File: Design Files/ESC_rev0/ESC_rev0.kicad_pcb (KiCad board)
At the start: 4 copper layers, 100 x 75 mm, 175 parts, among them J1 Conn_01x08, J2 Conn_01x06, J3 Conn_01x03, J4 WP-BUTR, J5 WP-BUTR, J6 WP-BUTR, J7 Conn_01x04, J8 Conn_01x06, J9 USB_C_Receptacle_USB2.0_16P, Q1 HSBA15810C, Q2 HSBA15810C, Q3 HSBA15810C, Q4 HSBA15810C, Q5 HSBA15810C, Q6 HSBA15810C, SW1 Push Button, U1 XT60PW-M, U2 XH-2PWBPZ, U3 AMS1117-3.3, U4 STM32F405RGTx, U5 DRV8302DCA, U6 ESDCAN24-2BLY, U7 SN65HVD230, Y1 Crystal

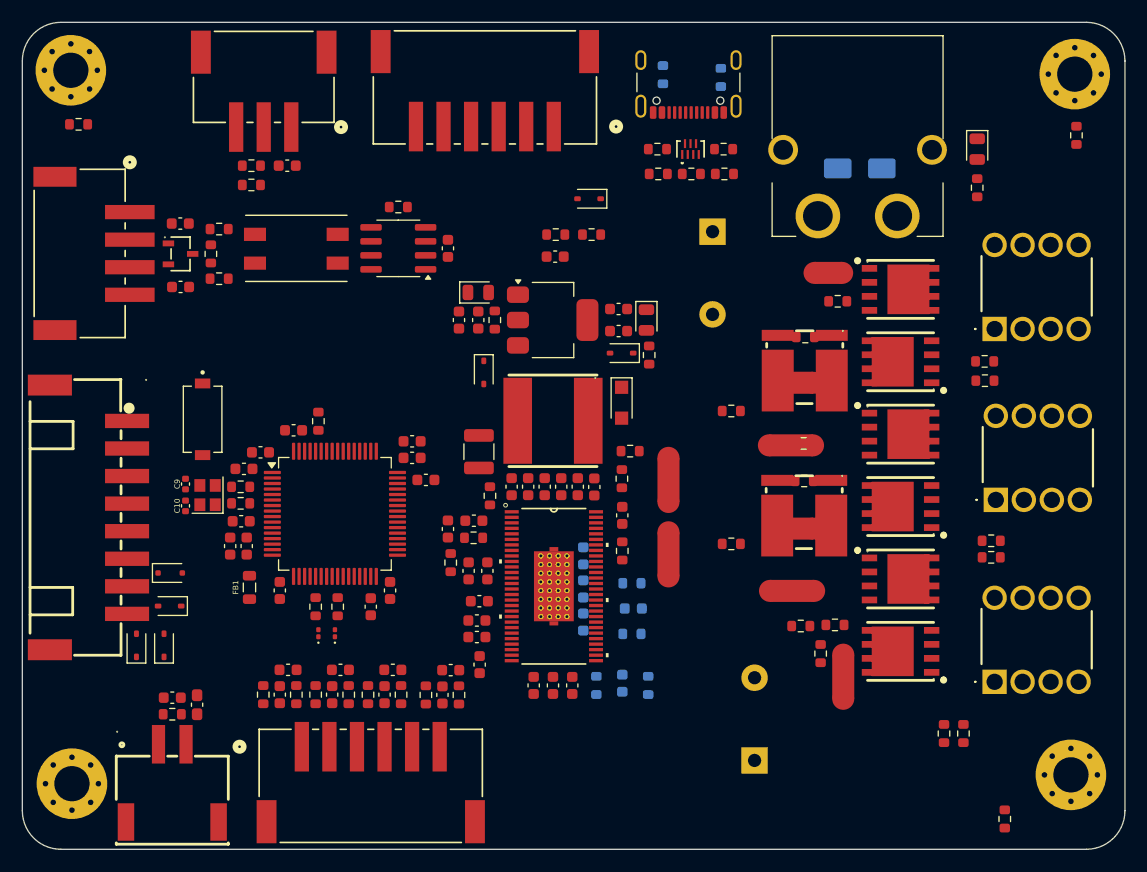
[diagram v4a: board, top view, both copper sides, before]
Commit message: update 18
Route process partially complete. Some corrections were made in footprints and pins references. Probably the power lines will need changes in size.
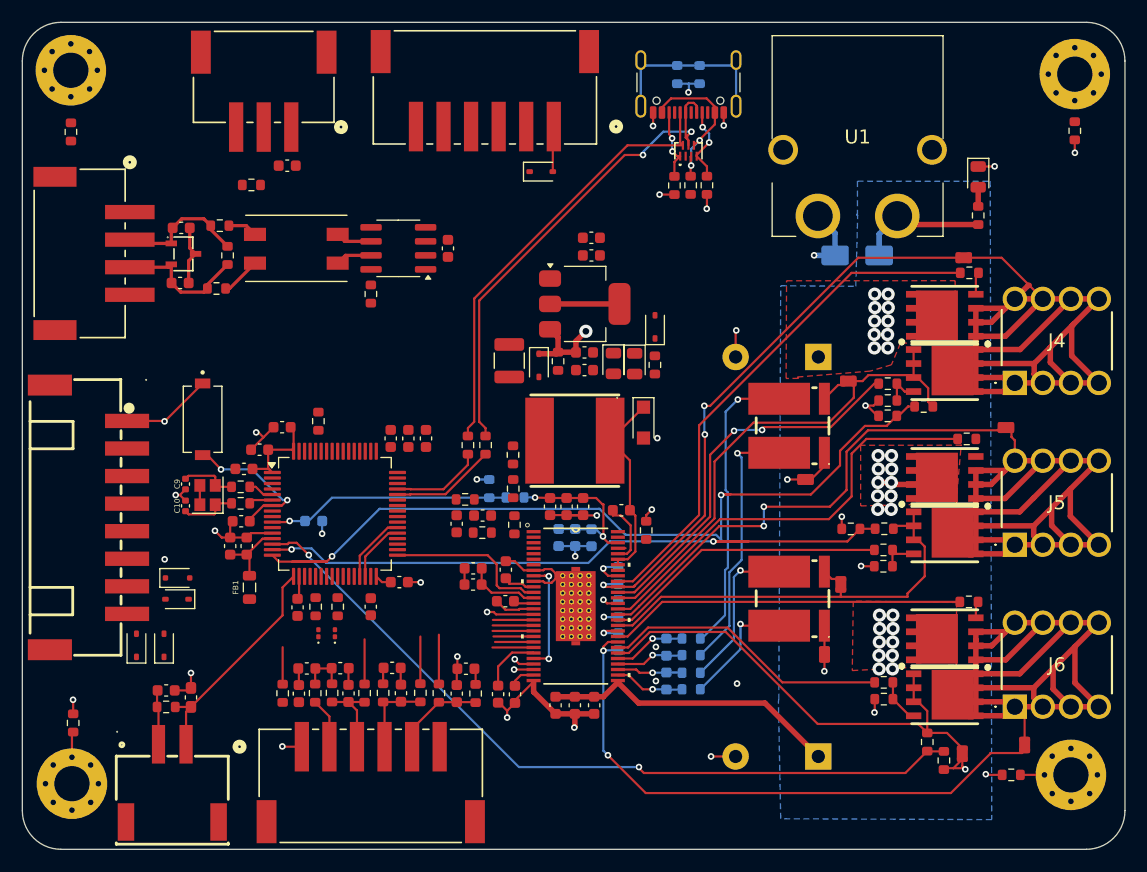
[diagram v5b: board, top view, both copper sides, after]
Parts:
- C38, C4, C44, C45, R2, R27, R3, R33, R52: moved to B.Cu
- NT1, NT2, NT5: footprint NetTie:NetTie-2_SMD_Pad2.00mm_Small -> NetTie:NetTie-2_SMD_Pad1.0mm_custom
- NT3, NT4, NT6, NT7, NT8: footprint NetTie:NetTie-2_SMD_Pad2.0mm -> NetTie:NetTie-2_SMD_Pad1.0mm_custom
- R29, R35, R54: moved to F.Cu
- moved R60 90.4 mm to (175.0, 64.9), turned to -90 degrees
- moved R62 84.9 mm to (84.2, 118.6), turned to 90 degrees
- moved R40 64.5 mm to (98.2, 76.2), turned to 90 degrees
- moved R52 61.5 mm to (141.0, 59.8), turned to -90 degrees
- moved R61 58.3 mm to (169.3, 123.3), turned to 180 degrees
- moved R59 53.2 mm to (84.0, 65.0), turned to -90 degrees
- moved R44 44.1 mm to (112.3, 115.9), turned to -90 degrees
- moved R19 36.6 mm to (161.7, 120.3)
- moved R13 35.9 mm to (119.8, 98.3), turned to 0 degrees
- moved R58 35.5 mm to (120.0, 93.4), turned to -90 degrees
- moved R57 32.8 mm to (121.6, 93.4), turned to -90 degrees
- moved C4 32.5 mm to (106.0, 100.3), turned to 0 degrees
- moved R27 29.2 mm to (140.2, 111.0)
- moved R29 28.5 mm to (158.1, 89.4)
- moved NT7 25.3 mm to (170.5, 120.6), turned to 90 degrees
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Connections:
- C38 pad 2: Net-(C38-Pad2) -> GND
- C40 pad 2: Net-(C38-Pad2) -> GND
- C41 pad 2: Net-(C38-Pad2) -> GND
- C42 pad 2: Net-(C38-Pad2) -> GND
- C44 pad 2: Net-(C38-Pad2) -> GND
- C45 pad 2: Net-(C38-Pad2) -> GND
- C53 pad 1: +3.3V -> +3V3
- C54 pad 1: +3.3V -> +3V3
- C57 pad 1: +3.3V -> +3V3
- C58 pad 1: +3.3V -> +3V3
- R44 pad 1: +3.3V -> +3V3
- R45 pad 1: +3.3V -> +3V3
- R48 pad 1: +3.3V -> +3V3
- R49 pad 1: +3.3V -> +3V3
- U1 pad 1: +VDC -> GND
- U1 pad 2: GND -> +VDC
- U4 pad 26: BR_S02 -> BR_SO2
- U4 pad 27: BR_S01 -> BR_SO1
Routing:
- net GND: track 0.00 -> 114.7 mm, vias 0 -> 39
- net /MOSFETs/PHASE_1: track 0.00 -> 92.8 mm
- net /MOSFETs/PHASE_3: track 0.00 -> 86.2 mm
- net /MOSFETs/PHASE_2: track 0.00 -> 84.4 mm
- net SENS1: track 0.00 -> 73.9 mm, vias 0 -> 2
- net SENS3: track 0.00 -> 70.8 mm, vias 0 -> 2
- net SENS2: track 0.00 -> 59.9 mm, vias 0 -> 2
- net +VDC: track 0.00 -> 59.5 mm, vias 0 -> 10
- net SH3: track 0.00 -> 53.7 mm, vias 0 -> 2
- net SH1: track 0.00 -> 51.9 mm, vias 0 -> 3
- net GH1: track 0.00 -> 47.4 mm
- net SH2: track 0.00 -> 46.4 mm, vias 0 -> 3
- net SL1: track 0.00 -> 45.3 mm
- net /USB/USB-C_N: track 0.00 -> 44.6 mm, vias 0 -> 2
- net SL3: track 0.00 -> 42.5 mm
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- added copper zone on B.Cu, net +VDC
- added copper zone on F.Cu, net +VDC

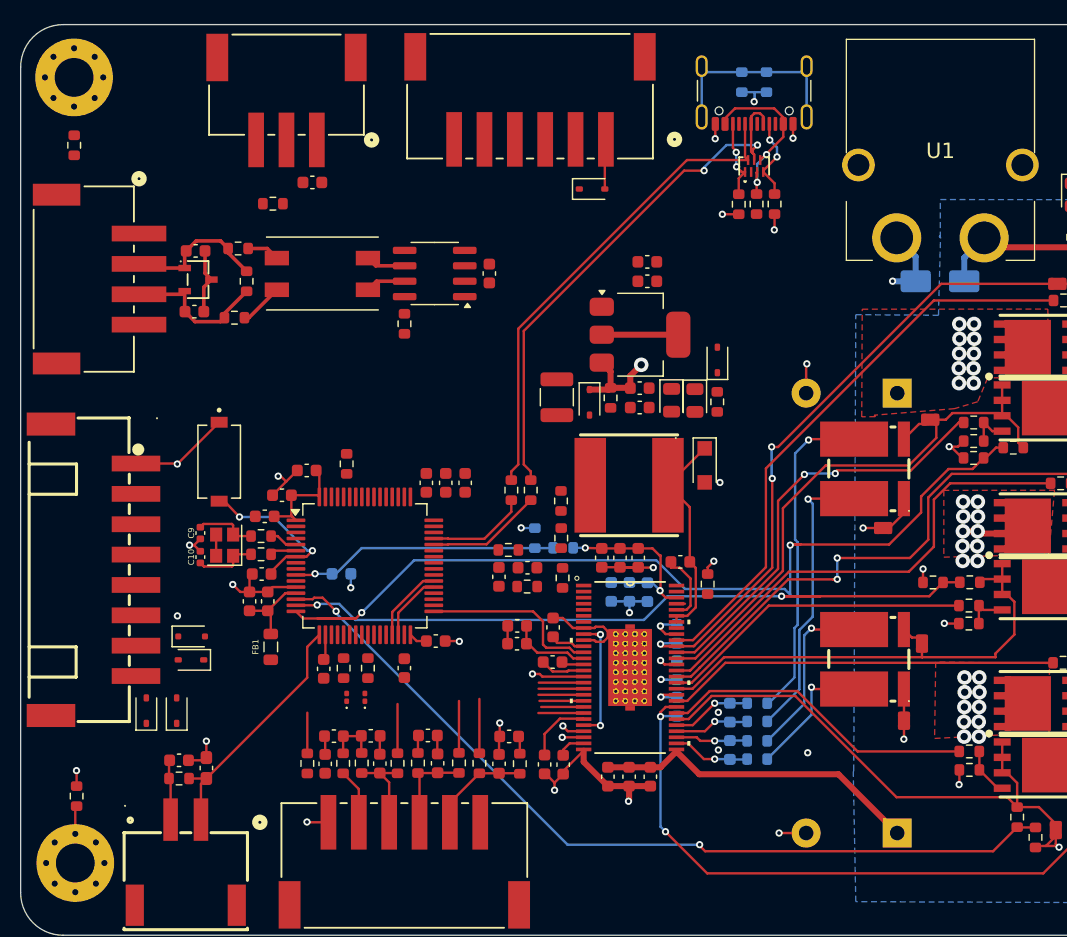
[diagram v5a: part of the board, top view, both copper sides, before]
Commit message: update 19
Preliminary routing finished, all signaling connections made.
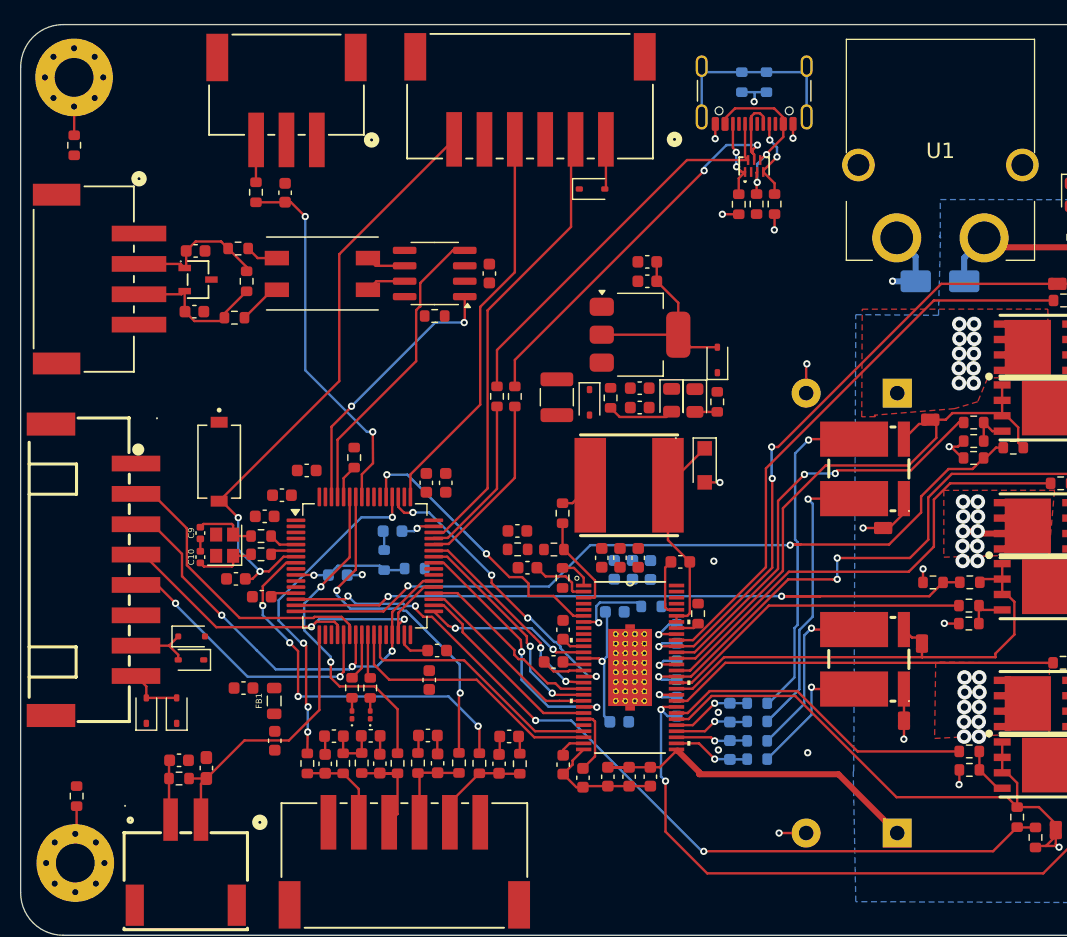
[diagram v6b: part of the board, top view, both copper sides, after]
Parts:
- C18, C26, C28, R14: moved to B.Cu
- moved R3 12.5 mm to (109.5, 99.2)
- moved R2 12.3 mm to (112.0, 99.9)
- moved C26 11.5 mm to (128.9, 112.5), turned to 0 degrees
- moved R14 10.4 mm to (131.5, 103.0), turned to 180 degrees
- moved C28 8.47 mm to (128.5, 103.4), turned to 0 degrees
- moved R57 7.83 mm to (120.3, 85.7)
- moved R58 7.81 mm to (118.8, 85.7)
- moved C18 7.18 mm to (110.2, 96.8), turned to 180 degrees
- moved C14 7.16 mm to (100.5, 114.0), turned to -90 degrees
- moved C22 7.16 mm to (97.9, 109.7), turned to 180 degrees
- moved FB1 4.46 mm to (100.5, 110.8)
- moved C27 4.07 mm to (120.5, 96.8), turned to 180 degrees
- moved C24 3.35 mm to (125.9, 117.1)
- moved C19 3.26 mm to (113.2, 109.0), turned to -90 degrees
- moved C16 3.06 mm to (113.9, 106.6), turned to 0 degrees
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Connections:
- U4 pad 61: /MCU/CAN_RX -> CAN_RX
- U4 pad 62: /MCU/CAN_TX -> CAN_TX
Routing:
- net GND: track 114.7 -> 57.0 mm, vias 39 -> 24
- net /MCU/SWDIO: track 0.00 -> 37.7 mm
- net /MCU/NRST: track 13.9 -> 50.0 mm
- net /MCU/SWCLK: track 0.00 -> 33.0 mm
- net /MCU/RX_SCL_MOSI: track 6.36 -> 38.3 mm, vias 0 -> 3
- net /MCU/SERVO: track 0.00 -> 30.6 mm, vias 0 -> 2
- net /MCU/TX_SDA_NSS: track 5.61 -> 35.9 mm, vias 0 -> 2
- net TEMP_OUT: track 4.47 -> 32.2 mm, vias 0 -> 4
- net CAN_RX: track 0.00 -> 25.2 mm
- net /MCU/MISO_ADC_EXT2: track 0.00 -> 24.7 mm
- net HALL_1_OUT: track 4.28 -> 28.9 mm, vias 0 -> 2
- net HALL_3_OUT: track 3.35 -> 27.7 mm, vias 0 -> 4
- net /MCU/SCK_ADC_EXT: track 0.00 -> 23.8 mm, vias 0 -> 2
- net FAULT: track 0.00 -> 23.7 mm, vias 0 -> 2
- net HALL_2_OUT: track 4.05 -> 27.4 mm, vias 0 -> 2
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
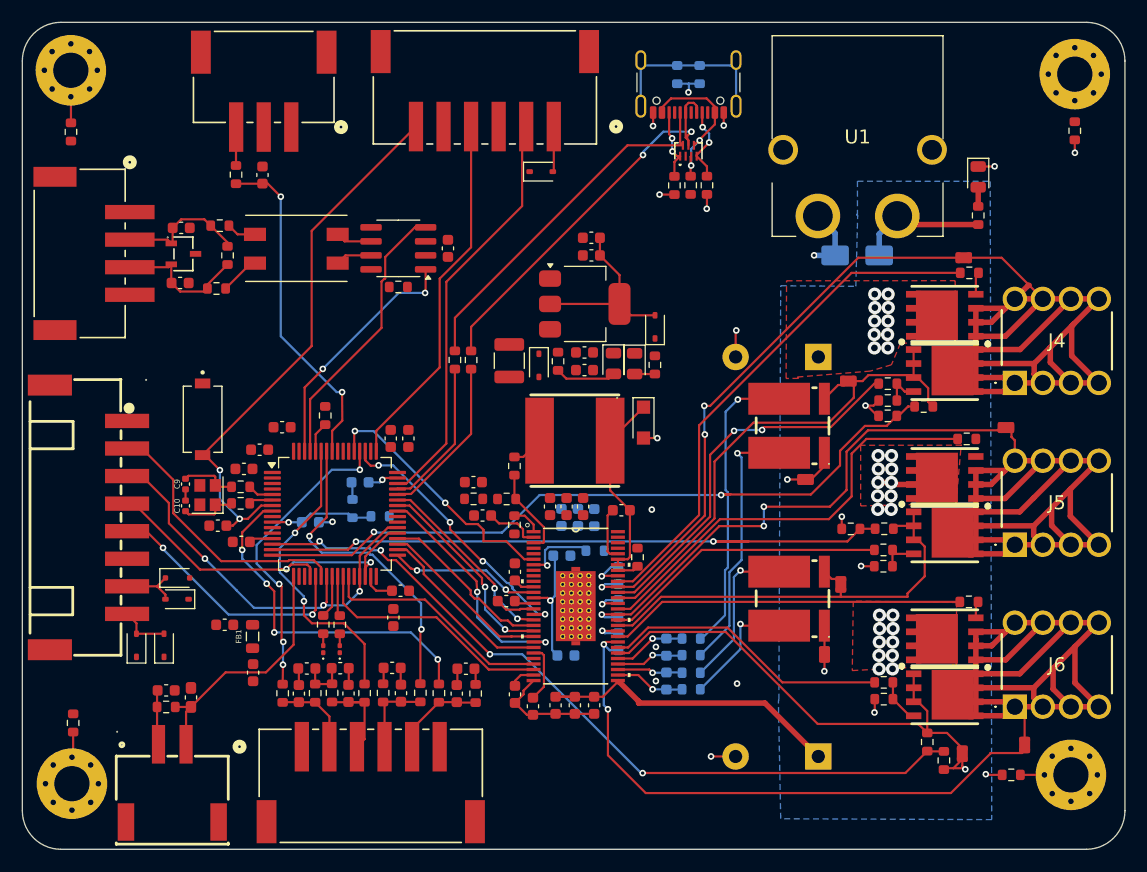
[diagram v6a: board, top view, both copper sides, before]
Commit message: update 20
Tracing complete (some power tracks need to be validated and some others optimizations weren't made). All connections were made, reference planes created, copper pour on mosfets and other power pads (not all). Some tracks were modified. References visible and apparently ok (it's just demo). Stitching vias were applied all over the board. Informative texts and symbols weren't included.
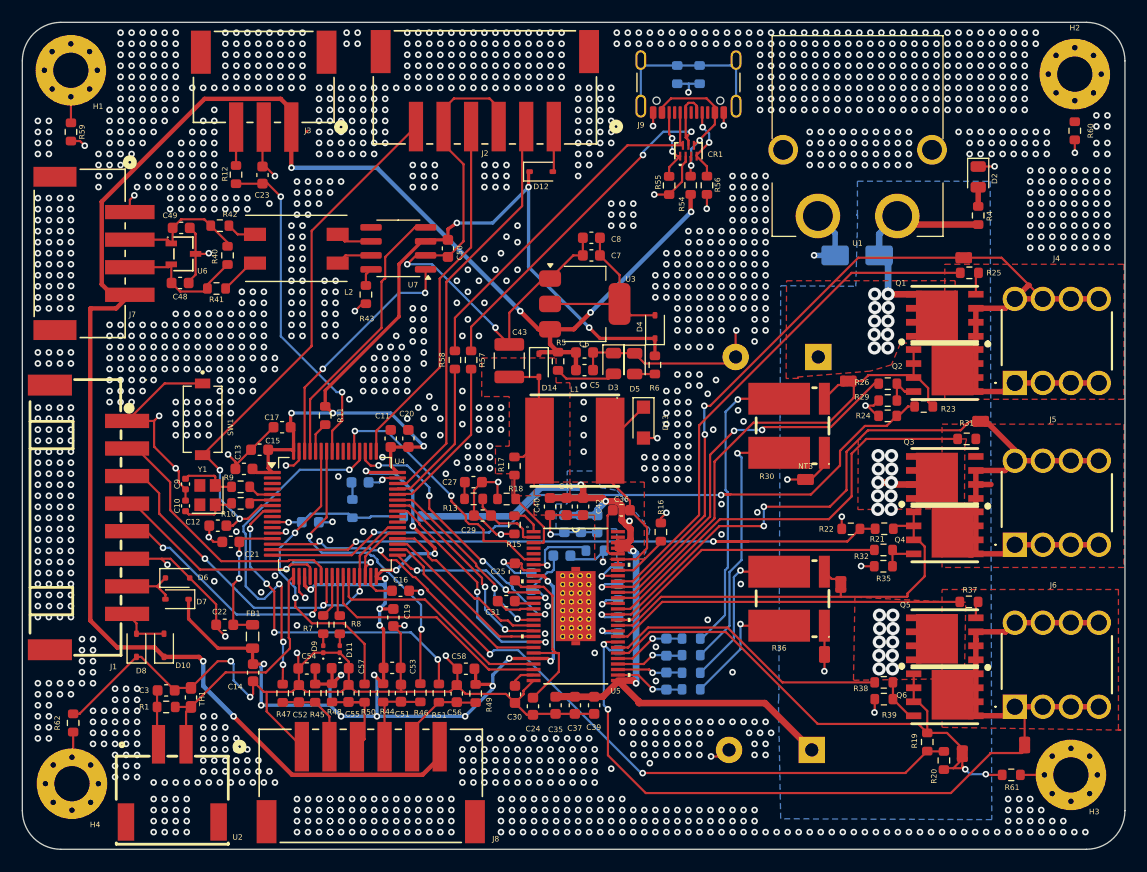
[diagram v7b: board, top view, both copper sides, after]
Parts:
- moved C26 7.40 mm to (125.8, 105.8), turned to 90 degrees
- moved R16 3.12 mm to (137.5, 101.3)
- moved R43 3.02 mm to (110.8, 79.8), turned to -90 degrees
- moved R2 2.96 mm to (115.0, 99.9)
- moved NT4 2.37 mm to (166.5, 91.2)
- moved C21 0.95 mm to (98.5, 102.2)
- moved C1 0.84 mm to (151.2, 121.0)
- moved C38 0.63 mm to (128.8, 100.5)
- moved C44 0.63 mm to (130.2, 100.5)
- moved C45 0.63 mm to (131.7, 100.5)
- moved R55 0.48 mm to (138.2, 69.9)
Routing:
- net GND: track 57.0 -> 298.1 mm, vias 24 -> 1790
- net +3V3: track 7.32 -> 197.1 mm, vias 0 -> 25
- net +5V: track 0.00 -> 165.7 mm, vias 0 -> 6
- net +VDC: track 44.3 -> 101.1 mm, vias 8 -> 35
- net /MOSFETs/PHASE_3: track 86.2 -> 34.6 mm
- net /MOSFETs/PHASE_1: track 92.8 -> 41.3 mm
- net /MOSFETs/PHASE_2: track 84.4 -> 37.2 mm
- net /MCU/+3V3_A: track 2.16 -> 12.8 mm, vias 0 -> 2
- net /MOSFET DRIVER/DVDD: track 7.22 -> 16.6 mm
- net /MOSFET DRIVER/+5V_x: track 2.89 -> 11.4 mm
- net HALL_3_OUT: track 27.7 -> 32.7 mm
- net Net-(U5-GVDD): track 11.2 -> 6.78 mm
- net /MOSFET DRIVER/BIAS: track 1.93 -> 5.28 mm
- net AN_IN: track 9.49 -> 12.4 mm
- net SH2: track 48.3 -> 46.2 mm
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- added copper zone on F.Cu, net +5V
- added copper zone on F.Cu, net /MOSFETs/PHASE_1
- added copper zone on F.Cu, net /MOSFETs/PHASE_2
- added copper zone on F.Cu, net /MOSFETs/PHASE_3
- added copper zone on In1.Cu, net GND
- added copper zone on In2.Cu, net GND
